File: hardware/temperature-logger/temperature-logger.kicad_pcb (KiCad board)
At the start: 2 copper layers, 40 x 30 mm, 20 parts, among them J1 Conn_01x05, U1 ATtiny85-20SU, U2 NCP1117-5.0_TO252, U3 MCP9801, U4 DS1307ZN+, U5 24FC512, Y1 Crystal

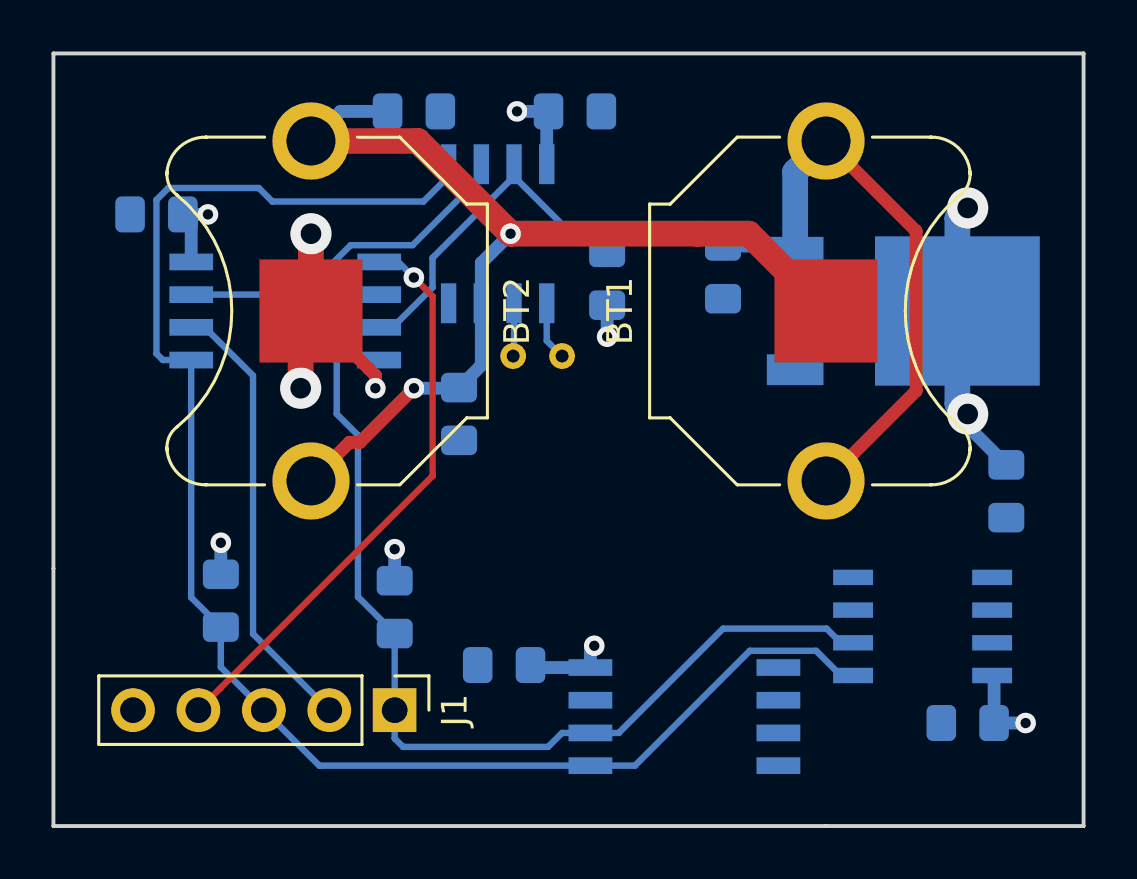
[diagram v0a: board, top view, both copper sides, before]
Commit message: finish pcb redesign
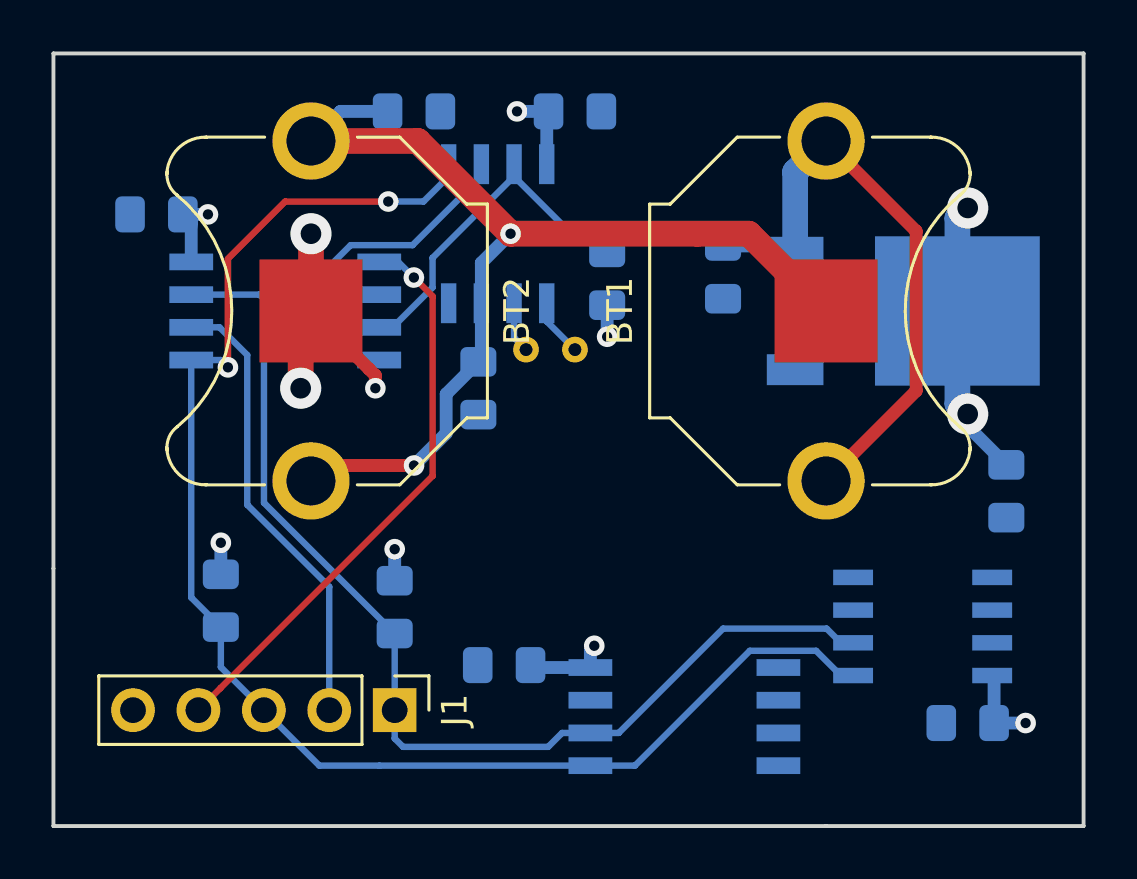
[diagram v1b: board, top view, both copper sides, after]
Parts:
- moved C8 1.25 mm to (96.5, 93.0)
- moved Y1 0.56 mm to (100.2, 91.5)
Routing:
- net /SDA: track 61.1 -> 57.1 mm, vias 0 -> 2
- net +BATT: track 40.2 -> 41.0 mm
- net /SCL: track 52.4 -> 53.1 mm
